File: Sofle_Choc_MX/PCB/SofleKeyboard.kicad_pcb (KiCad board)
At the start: 2 copper layers, 143.4 x 111.8 mm, 84 parts, among them J2 4PIN, J3 OLED, P1 i2c_pin, P2 i2c_pin, SW1 SW_PUSH_LED, SW10 SW_PUSH_LED, SW11 SW_PUSH_LED, SW12 SW_PUSH_LED, SW13 SW_PUSH_LED, SW14 SW_PUSH_LED, SW15 SW_PUSH_LED, SW16 SW_PUSH_LED, SW17 SW_PUSH_LED, SW18 SW_PUSH_LED, SW19 SW_PUSH_LED, SW2 SW_PUSH_LED, SW20 SW_PUSH_LED, SW21 SW_PUSH_LED, SW22 SW_PUSH_LED, SW23 SW_PUSH_LED, SW24 SW_PUSH_LED, SW25 Rotary_Encoder_Switch, SW26 SW_PUSH_LED, SW27 SW_PUSH_LED, SW28 SW_PUSH_LED, SW29 SW_PUSH_LED, SW3 SW_PUSH_LED, SW30 SW_PUSH_LED, SW4 SW_PUSH_LED, SW5 SW_PUSH_LED, SW6 SW_PUSH_LED, SW7 SW_PUSH_LED, SW8 SW_PUSH_LED, SW9 SW_PUSH_LED, U1 ProMicro

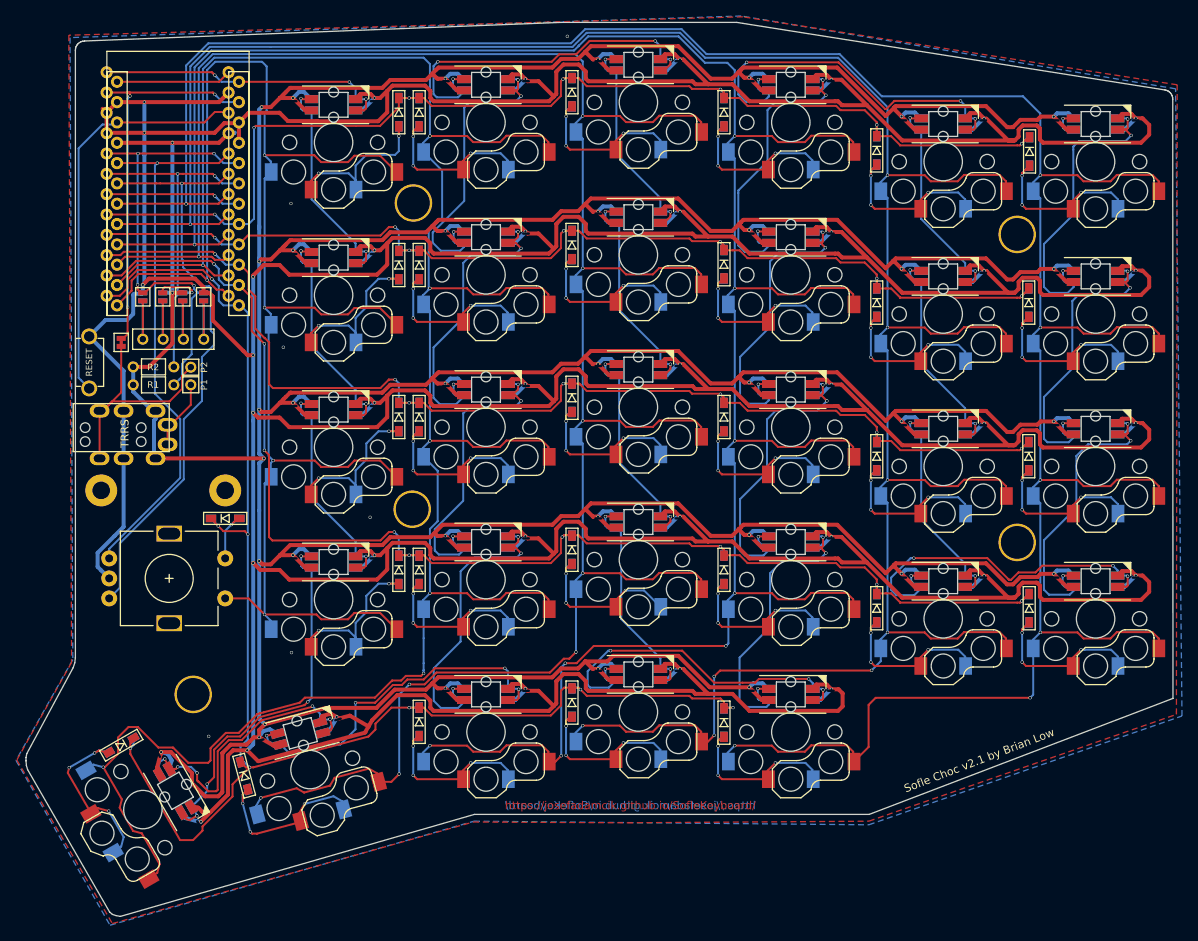
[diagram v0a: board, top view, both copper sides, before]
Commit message: Tied front zone to VCC Updated LED footprint with compact DS variant
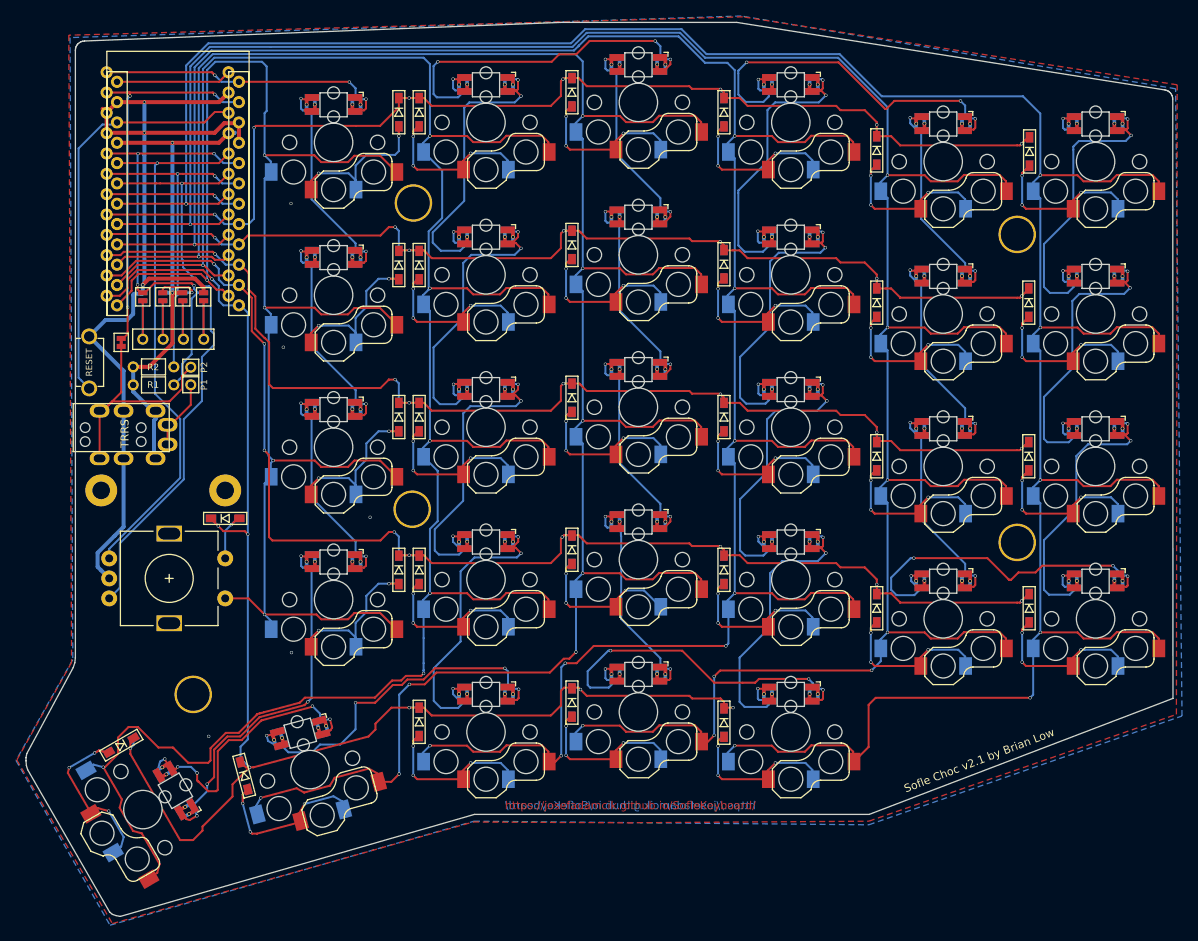
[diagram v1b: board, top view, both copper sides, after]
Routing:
- net GND: track 1090.4 -> 117.2 mm, vias 43 -> 8
- net VCC: track 889.9 -> 64.9 mm, vias 37 -> 2
- added copper zone on F.Cu, net VCC
- removed copper zone on F.Cu, net GND

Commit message: Swapped out SMD Diode footprint for through-hole SMD hybrid footprint
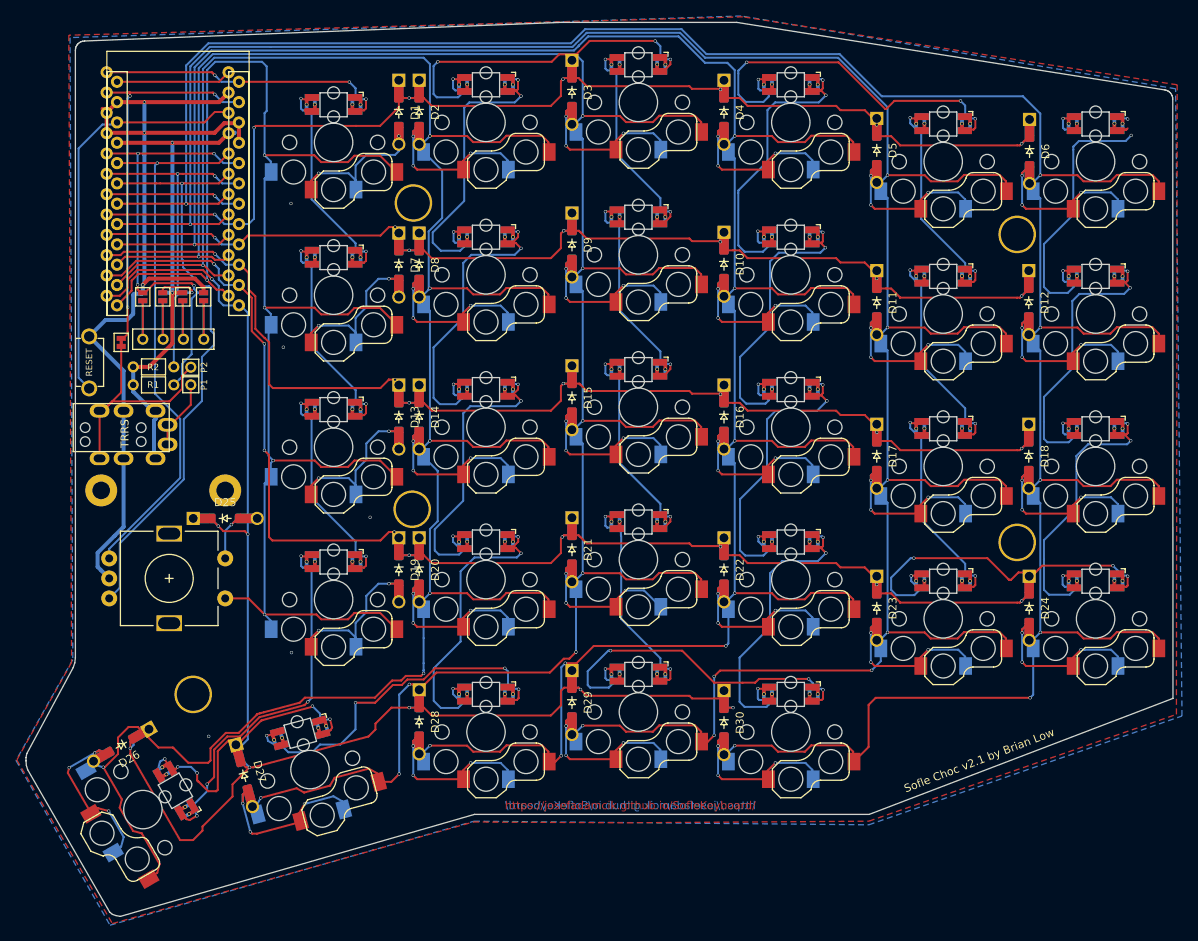
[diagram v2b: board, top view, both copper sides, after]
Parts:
- D1, D10, D11, D12, D13, D14, D15, D16, D17, D18, D19, D2, D20, D21, D22, D23, D24, D25, D26, D27, D28, D29, D3, D30, D4, D5, D6, D7, D8, D9: footprint Diode_SMD:crkbd-diode -> SofleChoc:D_SOD-123_DO-35_Hybrid_DoubleSided
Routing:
- net Net-(SW12-Pad2): track 41.7 -> 39.5 mm

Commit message: Wiped switch vias and traces for reroute
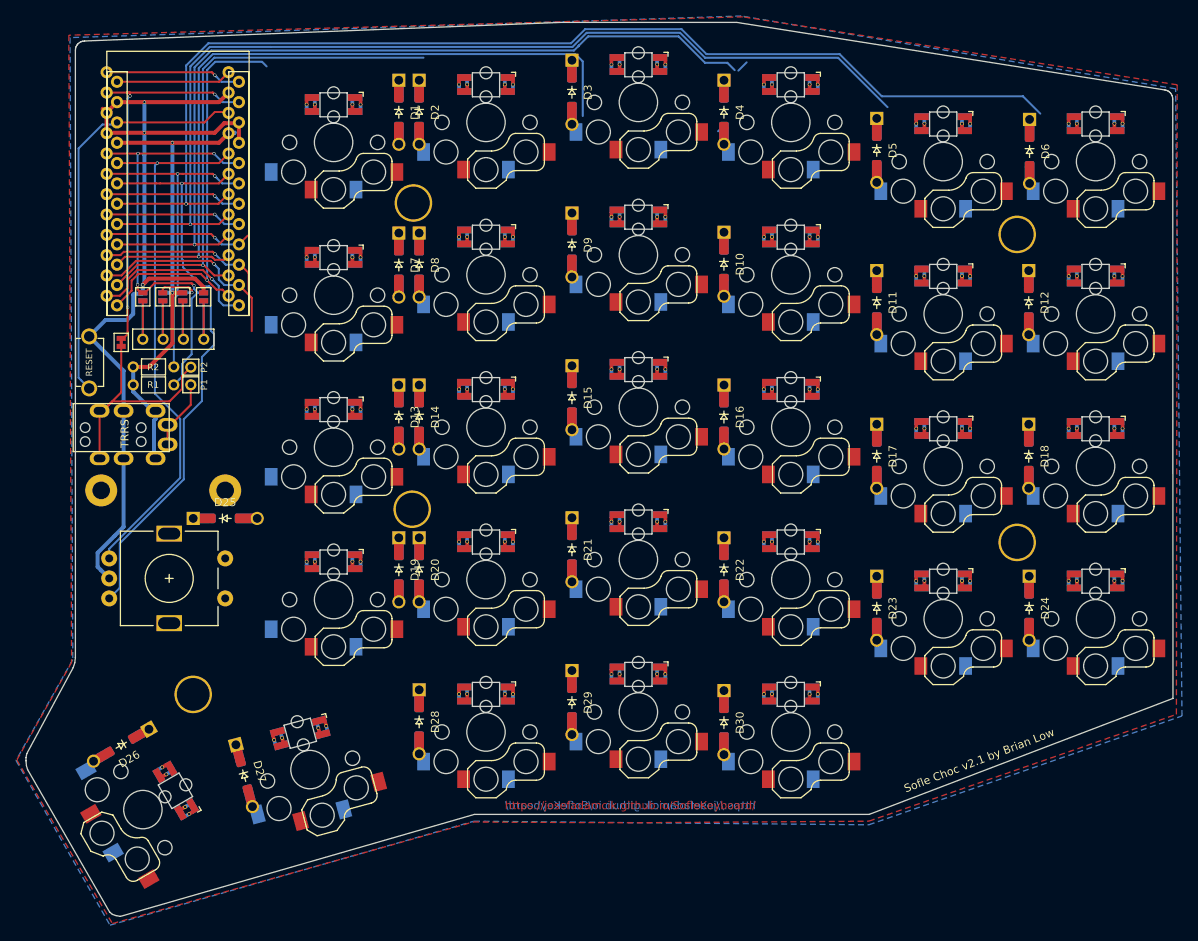
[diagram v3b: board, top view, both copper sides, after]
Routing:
- net col4: track 288.6 -> 68.7 mm, vias 7 -> 1
- net col2: track 304.4 -> 107.8 mm, vias 9 -> 1
- net col3: track 290.9 -> 95.2 mm, vias 9 -> 1
- net col0: track 336.6 -> 145.0 mm, vias 7 -> 1
- net col1: track 317.4 -> 126.9 mm, vias 9 -> 1
- net row4: track 189.5 -> 21.6 mm, vias 8 -> 1
- net SW25A: track 201.0 -> 51.9 mm, vias 5 -> 1
- net row3: track 166.8 -> 25.8 mm, vias 9 -> 1
- net row0: track 145.8 -> 18.3 mm, vias 7 -> 1
- net row2: track 147.9 -> 21.1 mm, vias 7 -> 1
- net row1: track 135.0 -> 18.6 mm, vias 7 -> 1
- net Net-(SW4-Pad2): track 49.5 -> 1.47 mm, vias 4 -> 0
- net Net-(SW19-Pad2): track 47.0 -> 0.00 mm, vias 4 -> 0
- net Net-(SW2-Pad2): track 47.0 -> 0.00 mm, vias 4 -> 0
- net Net-(SW29-Pad2): track 45.5 -> 0.00 mm, vias 4 -> 0
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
